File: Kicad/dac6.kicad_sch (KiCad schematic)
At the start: 13 parts

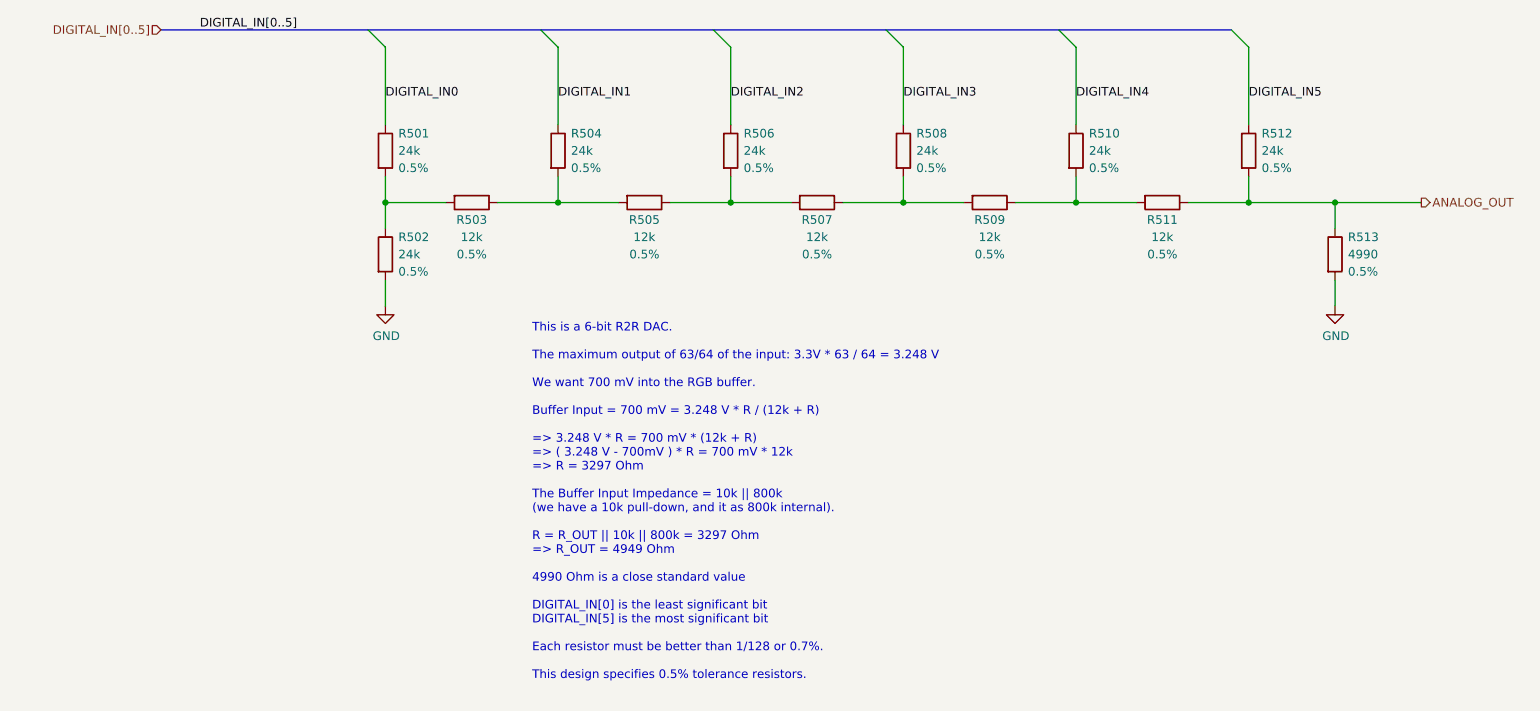
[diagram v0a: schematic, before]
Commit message: Update schematic files to Kicad 6.
Had to fix some symbols which didn't have perfect matches in K6.
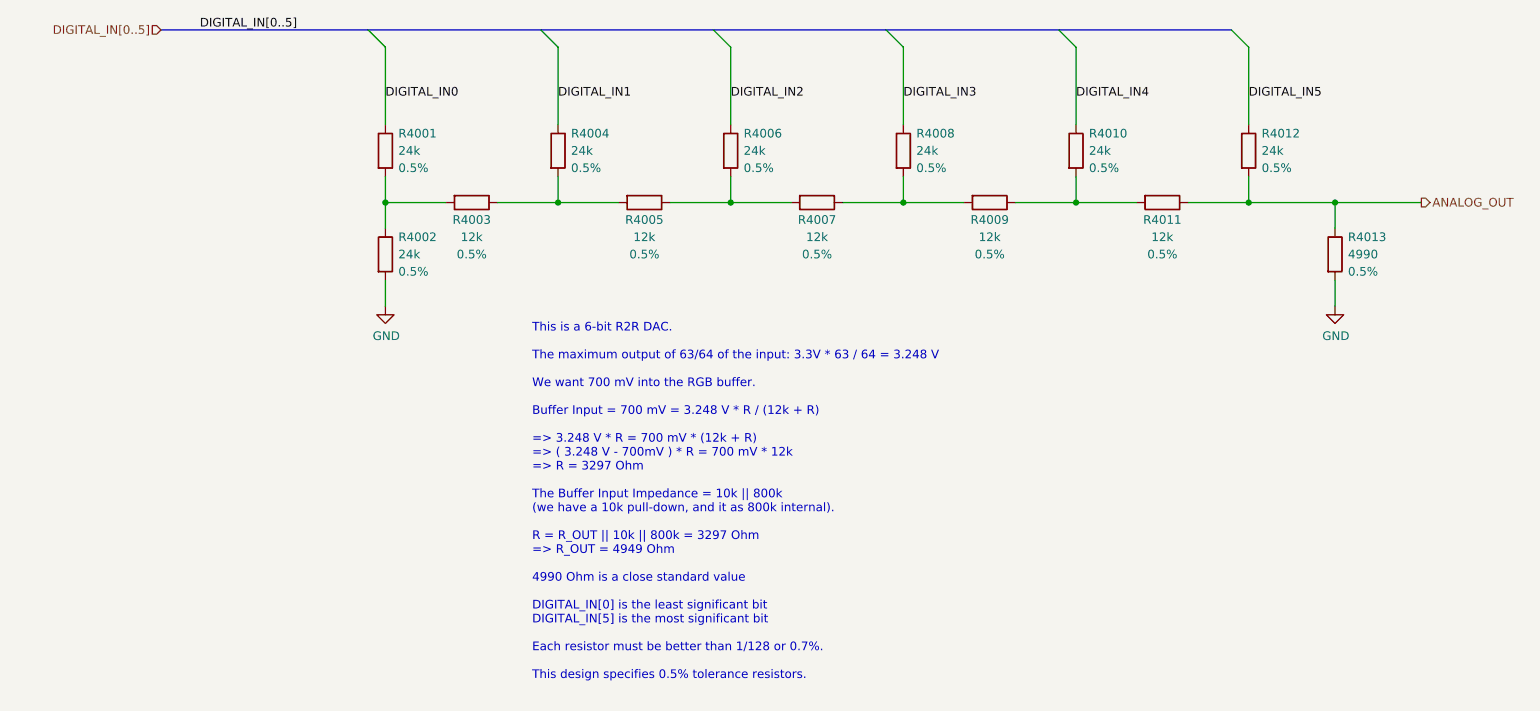
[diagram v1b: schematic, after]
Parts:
- renumbered R501 to R4001, R502 to R4002, R503 to R4003, R504 to R4004, R505 to R4005, R506 to R4006, R507 to R4007, R508 to R4008, R509 to R4009, R510 to R4010, R511 to R4011, R512 to R4012, R513 to R4013
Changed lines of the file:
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@@
   (symbol (lib_id "Device:R") (at 101.6 76.2 270) (unit 1)
     (in_bom yes) (on_board yes)
-    (property "Reference" "R503" (id 0) (at 101.6 78.74 90))
+    (property "Reference" "R4003" (id 0) (at 101.6 78.74 90))
     (property "Value" "12k" (id 1) (at 101.6 81.28 90))
     (property "Footprint" "Resistor_SMD:R_0805_2012Metric_Pad1.20x1.40mm_HandSolder" (id 2) (at 101.6 74.422 90)
@@
   (symbol (lib_id "Device:R") (at 228.6 83.82 0) (unit 1)
     (in_bom yes) (on_board yes)
-    (property "Reference" "R513" (id 0) (at 230.505 81.28 0)
+    (property "Reference" "R4013" (id 0) (at 230.505 81.28 0)
       (effects (font (size 1.27 1.27)) (justify left))
     )
@@
   (symbol (lib_id "power:GND") (at 88.9 91.44 0) (unit 1)
     (in_bom yes) (on_board yes)
-    (property "Reference" "#PWR0501" (id 0) (at 88.9 97.79 0)
+    (property "Reference" "#PWR04001" (id 0) (at 88.9 97.79 0)
       (effects (font (size 1.27 1.27)) hide)
     )
@@
   (symbol (lib_id "power:GND") (at 228.6 91.44 0) (unit 1)
     (in_bom yes) (on_board yes)
-    (property "Reference" "#PWR0502" (id 0) (at 228.6 97.79 0)
+    (property "Reference" "#PWR04002" (id 0) (at 228.6 97.79 0)
       (effects (font (size 1.27 1.27)) hide)
     )
@@
   (symbol (lib_id "Device:R") (at 88.9 68.58 0) (unit 1)
     (in_bom yes) (on_board yes)
-    (property "Reference" "R501" (id 0) (at 90.805 66.04 0)
+    (property "Reference" "R4001" (id 0) (at 90.805 66.04 0)
       (effects (font (size 1.27 1.27)) (justify left))
     )
@@
   (symbol (lib_id "Device:R") (at 114.3 68.58 0) (unit 1)
     (in_bom yes) (on_board yes)
-    (property "Reference" "R504" (id 0) (at 116.205 66.04 0)
+    (property "Reference" "R4004" (id 0) (at 116.205 66.04 0)
       (effects (font (size 1.27 1.27)) (justify left))
     )
@@
   (symbol (lib_id "Device:R") (at 139.7 68.58 0) (unit 1)
     (in_bom yes) (on_board yes)
-    (property "Reference" "R506" (id 0) (at 141.605 66.04 0)
+    (property "Reference" "R4006" (id 0) (at 141.605 66.04 0)
       (effects (font (size 1.27 1.27)) (justify left))
     )
@@
   (symbol (lib_id "Device:R") (at 165.1 68.58 0) (unit 1)
     (in_bom yes) (on_board yes)
-    (property "Reference" "R508" (id 0) (at 167.005 66.04 0)
+    (property "Reference" "R4008" (id 0) (at 167.005 66.04 0)
       (effects (font (size 1.27 1.27)) (justify left))
     )
@@
   (symbol (lib_id "Device:R") (at 190.5 68.58 0) (unit 1)
     (in_bom yes) (on_board yes)
-    (property "Reference" "R510" (id 0) (at 192.405 66.04 0)
+    (property "Reference" "R4010" (id 0) (at 192.405 66.04 0)
       (effects (font (size 1.27 1.27)) (justify left))
     )
@@
   (symbol (lib_id "Device:R") (at 215.9 68.58 0) (unit 1)
     (in_bom yes) (on_board yes)
-    (property "Reference" "R512" (id 0) (at 217.805 66.04 0)
+    (property "Reference" "R4012" (id 0) (at 217.805 66.04 0)
       (effects (font (size 1.27 1.27)) (justify left))
     )
@@
   (symbol (lib_id "Device:R") (at 88.9 83.82 0) (unit 1)
     (in_bom yes) (on_board yes)
-    (property "Reference" "R502" (id 0) (at 90.805 81.28 0)
+    (property "Reference" "R4002" (id 0) (at 90.805 81.28 0)
       (effects (font (size 1.27 1.27)) (justify left))
     )
@@
   (symbol (lib_id "Device:R") (at 127 76.2 270) (unit 1)
     (in_bom yes) (on_board yes)
-    (property "Reference" "R505" (id 0) (at 127 78.74 90))
+    (property "Reference" "R4005" (id 0) (at 127 78.74 90))
     (property "Value" "12k" (id 1) (at 127 81.28 90))
     (property "Footprint" "Resistor_SMD:R_0805_2012Metric_Pad1.20x1.40mm_HandSolder" (id 2) (at 127 74.422 90)
@@
   (symbol (lib_id "Device:R") (at 152.4 76.2 270) (unit 1)
     (in_bom yes) (on_board yes)
-    (property "Reference" "R507" (id 0) (at 152.4 78.74 90))
+    (property "Reference" "R4007" (id 0) (at 152.4 78.74 90))
     (property "Value" "12k" (id 1) (at 152.4 81.28 90))
     (property "Footprint" "Resistor_SMD:R_0805_2012Metric_Pad1.20x1.40mm_HandSolder" (id 2) (at 152.4 74.422 90)
@@
   (symbol (lib_id "Device:R") (at 177.8 76.2 270) (unit 1)
     (in_bom yes) (on_board yes)
-    (property "Reference" "R509" (id 0) (at 177.8 78.74 90))
+    (property "Reference" "R4009" (id 0) (at 177.8 78.74 90))
     (property "Value" "12k" (id 1) (at 177.8 81.28 90))
     (property "Footprint" "Resistor_SMD:R_0805_2012Metric_Pad1.20x1.40mm_HandSolder" (id 2) (at 177.8 74.422 90)
@@
   (symbol (lib_id "Device:R") (at 203.2 76.2 270) (unit 1)
     (in_bom yes) (on_board yes)
-    (property "Reference" "R511" (id 0) (at 203.2 78.74 90))
+    (property "Reference" "R4011" (id 0) (at 203.2 78.74 90))
     (property "Value" "12k" (id 1) (at 203.2 81.28 90))
     (property "Footprint" "Resistor_SMD:R_0805_2012Metric_Pad1.20x1.40mm_HandSolder" (id 2) (at 203.2 74.422 90)

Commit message: Imported sheets from Neotron Pico.
Standardised on +3V3 not +3.3V
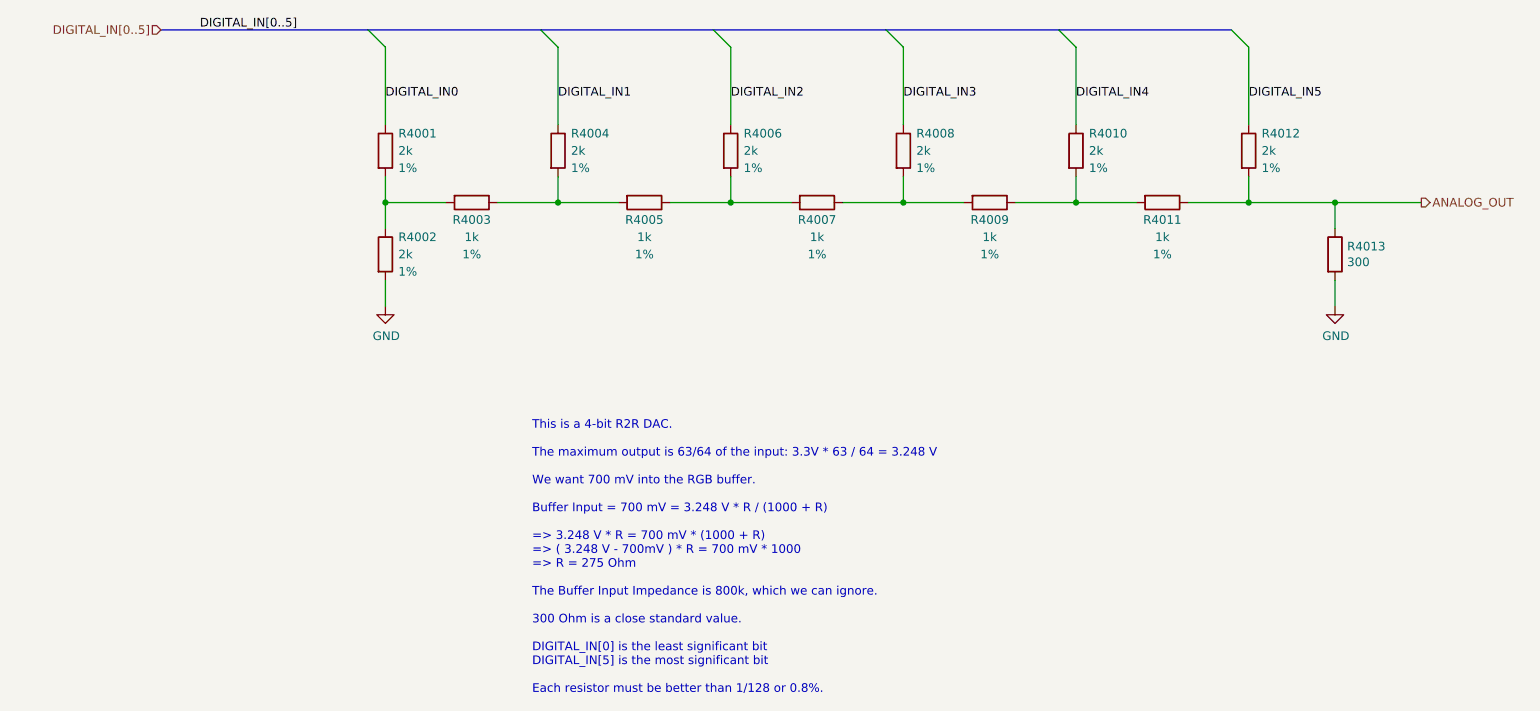
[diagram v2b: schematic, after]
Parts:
- R4001, R4002, R4004, R4006, R4008, R4010, R4012: value 24k -> 2k; Digikey RNCF0805DTE24K0CT-ND -> (none); JLCPCB Collection (none) -> Basic; LCSC Part# (none) -> C17604; MPN RNCF0805DTE24K0 -> 0805W8F2001T5E; Manufacturer Stackpole -> Uniroyal; Tolerance 0.5% -> 1%
- R4003, R4005, R4007, R4009, R4011: value 12k -> 1k; Digikey RNCF0805DTE12K0CT-ND -> (none); JLCPCB Collection (none) -> Basic; LCSC Part# (none) -> C17513; MPN RNCF0805DTE12K0 -> 0805W8F1001T5E; Manufacturer Stackpole -> Uniroyal; Tolerance 0.5% -> 1%
- R4013: value 4990 -> 300; Digikey RNCF0805DTE4K99CT-ND -> (none); JLCPCB Collection (none) -> Basic; LCSC Part# (none) -> C17617; MPN RNCF0805DTE4K99 -> 0805W8F3000T5E; Manufacturer Stackpole -> Uniroyal; Tolerance 0.5% -> 1%
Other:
- note added: "This is a 4-bit R2R DAC. The maximum output is 63/64 of the input: 3.3V * 63 / 64 = 3.248 V We want 700 mV into the RGB buffer. Buffer Input = 700 mV = 3.248 V * R / (1000 + R) => 3.248 V * R = 700 mV * (1000 + R) => ( 3.248 V - 700mV ) * R = 700 mV * 1000 => R = 275 Ohm The Buffer Input Impedance is 800k, which we can ignore. 300 Ohm is a close standard value. DIGITAL_IN[0] is the least signific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"
- note removed: "This is a 6-bit R2R DAC. The maximum output of 63/64 of the input: 3.3V * 63 / 64 = 3.248 V We want 700 mV into the RGB buffer. Buffer Input = 700 mV = 3.248 V * R / (12k + R) => 3.248 V * R = 700 mV * (12k + R) => ( 3.248 V - 700mV ) * R = 700 mV * 12k => R = 3297 Ohm The Buffer Input Impedance = 10k || 800k (we have a 10k pull-down, and it as 800k internal). R = R_OUT || 10k || 800k = 3297 Ohm 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"
